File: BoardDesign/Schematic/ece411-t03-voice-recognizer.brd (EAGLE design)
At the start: 92.7 x 63.5 mm, 52 parts, among them J1 5.5x2.1mm Barrel, Q1 16MHz, X1 USB-A

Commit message: asdf
asdasfsadfsfd
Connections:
- net N$7: now also J1.VIN0, SERVO_OUT.1, V_BARREL.TP; no longer TP_USB.TP, X1.1
- net VCC: now also TP_USB.TP, X1.1; no longer J1.VIN0, SERVO_OUT.1, V_BARREL.TP
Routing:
- net VCC: track 295.6 -> 287.8 mm
- net N$7: track 7.74 -> 4.99 mm
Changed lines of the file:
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@@
 <wire x1="53.34" y1="29.87" x2="56.43" y2="29.87" width="0.508" layer="1"/>
 <wire x1="85.09" y1="44.45" x2="82.55" y2="41.91" width="1.27" layer="1"/>
-<contactref element="J1" pad="VIN0"/>
-<contactref element="SERVO_OUT" pad="1"/>
-<contactref element="V_BARREL" pad="TP"/>
 <wire x1="63.5" y1="7.62" x2="63.5" y2="2.54" width="1.27" layer="1"/>
 <wire x1="68.03" y1="23.47" x2="65.43" y2="23.47" width="0.508" layer="1"/>
-<wire x1="95.25" y1="55.23" x2="90.17" y2="55.23" width="1.27" layer="1"/>
-<wire x1="95.25" y1="58.42" x2="96.52" y2="59.69" width="1.27" layer="1"/>
-<wire x1="95.25" y1="58.42" x2="95.25" y2="55.23" width="1.27" layer="1"/>
 <wire x1="90.17" y1="55.23" x2="87.63" y2="52.69" width="1.27" layer="1"/>
-<wire x1="87.63" y1="52.69" x2="87.63" y2="50.8" width="1.27" layer="1"/>
 <contactref element="C9" pad="1"/>
 <contactref element="U$1" pad="44"/>
@@
 <wire x1="35.69" y1="36.83" x2="35.69" y2="52.2" width="1.27" layer="1"/>
 <wire x1="35.69" y1="52.2" x2="38.1" y2="54.61" width="1.27" layer="1"/>
-<wire x1="90.17" y1="48.26" x2="87.63" y2="50.8" width="0.508" layer="1"/>
 <wire x1="54.74" y1="11.43" x2="54.61" y2="11.56" width="0.508" layer="1"/>
 <wire x1="54.74" y1="11.43" x2="57.15" y2="11.43" width="0.508" layer="1"/>
@@
 <via x="90.17" y="39.37" extent="1-16" drill="0.35"/>
 <wire x1="90.17" y1="39.37" x2="90.17" y2="48.26" width="0.508" layer="1"/>
+<contactref element="X1" pad="1"/>
+<contactref element="TP_USB" pad="TP"/>
+<wire x1="90.17" y1="22.86" x2="87.57" y2="20.26" width="0.508" layer="1"/>
+<wire x1="87.57" y1="16.2" x2="87.57" y2="20.26" width="0.508" layer="1"/>
+<wire x1="87.63" y1="52.69" x2="90.17" y2="48.26" width="0" layer="19" extent="1-1"/>
+<wire x1="90.17" y1="22.86" x2="90.17" y2="39.37" width="0" layer="19" extent="1-1"/>
 </signal>
 <signal name="SIGNAL">
@@
 <wire x1="67.31" y1="33.55" x2="67.31" y2="35.56" width="0.508" layer="1"/>
 <wire x1="67.31" y1="35.56" x2="69.85" y2="38.1" width="0.508" layer="1"/>
-</signal>
-<signal name="N$7">
-<contactref element="X1" pad="1"/>
-<contactref element="TP_USB" pad="TP"/>
-<wire x1="90.17" y1="22.86" x2="87.57" y2="20.26" width="0.508" layer="1"/>
-<wire x1="87.57" y1="16.2" x2="87.57" y2="20.26" width="0.508" layer="1"/>
 </signal>
 <signal name="MISO">
@@
 <wire x1="38.1" y1="29.21" x2="35.69" y2="31.75" width="0.508" layer="1"/>
 </signal>
+<signal name="N$7">
+<contactref element="J1" pad="VIN0"/>
+<contactref element="SERVO_OUT" pad="1"/>
+<contactref element="V_BARREL" pad="TP"/>
+<wire x1="95.25" y1="58.42" x2="96.52" y2="59.69" width="1.27" layer="1"/>
+<wire x1="95.25" y1="58.42" x2="95.25" y2="55.23" width="1.27" layer="1"/>
+<wire x1="87.63" y1="50.8" x2="95.25" y2="55.23" width="0" layer="19" extent="1-1"/>
+</signal>
 </signals>

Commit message: Final final finalize finale of the final board layout
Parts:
- removed X1: USB-A, adafruit:MOLEX_480371000
- added J2: USB_MINI-B_SMT, SparkFun-Connectors:USB-MINIB
- moved TP_USB 17.8 mm to (91.4, 5.08)
- moved USB_TO_GND 14.5 mm to (90.2, 17.8)
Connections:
- net GND: now also J2.GND; no longer X1.4
- net N$3: now also J2.D+; no longer X1.3
- net N$9: now also J2.D-; no longer X1.2
- net VCC: now also J2.VBUS; no longer X1.1
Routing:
- net VCC: track 287.8 -> 339.4 mm, vias 4 -> 6
- net GND: track 401.9 -> 388.3 mm
- net N$7: track 4.99 -> 15.5 mm
- net N$9: track 8.37 -> 18.9 mm
- net N$3: track 21.0 -> 23.3 mm, vias 2 -> 1

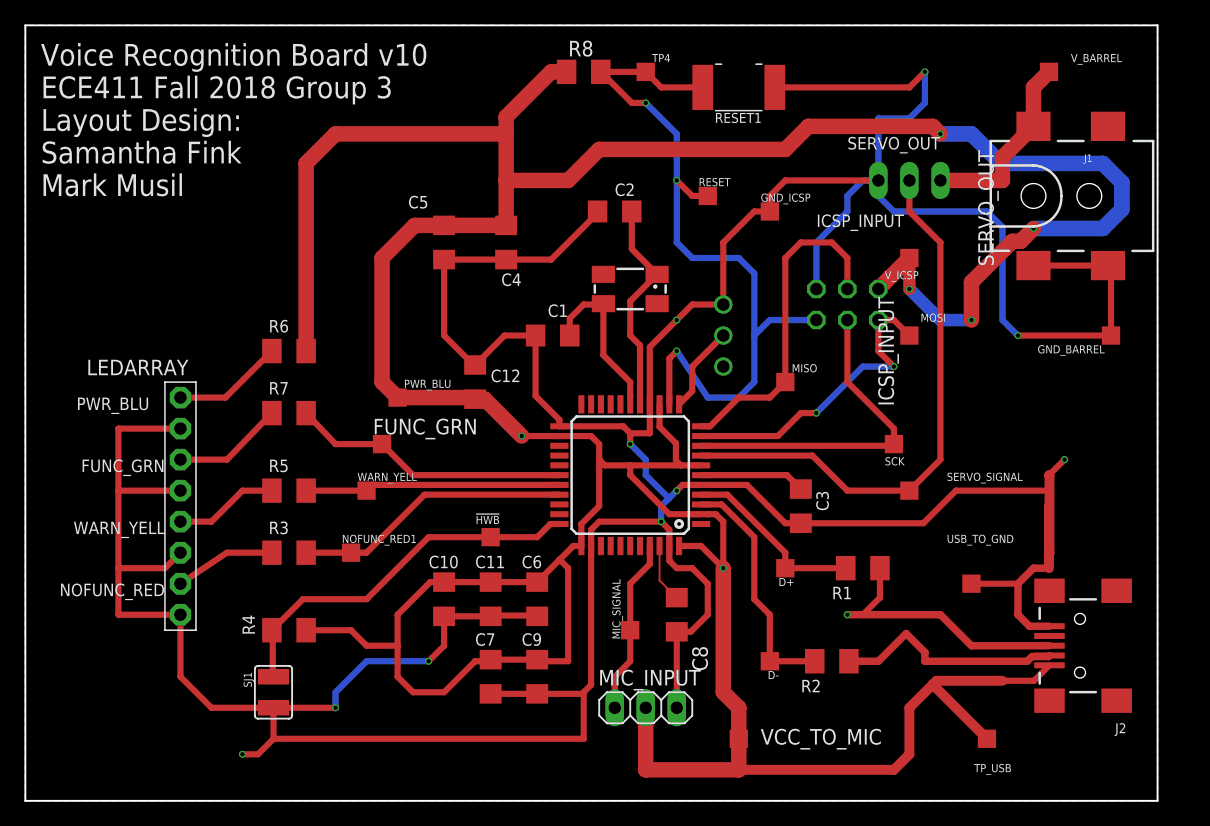
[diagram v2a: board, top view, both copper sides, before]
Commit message: ERC/DRC Checks Complete on new board
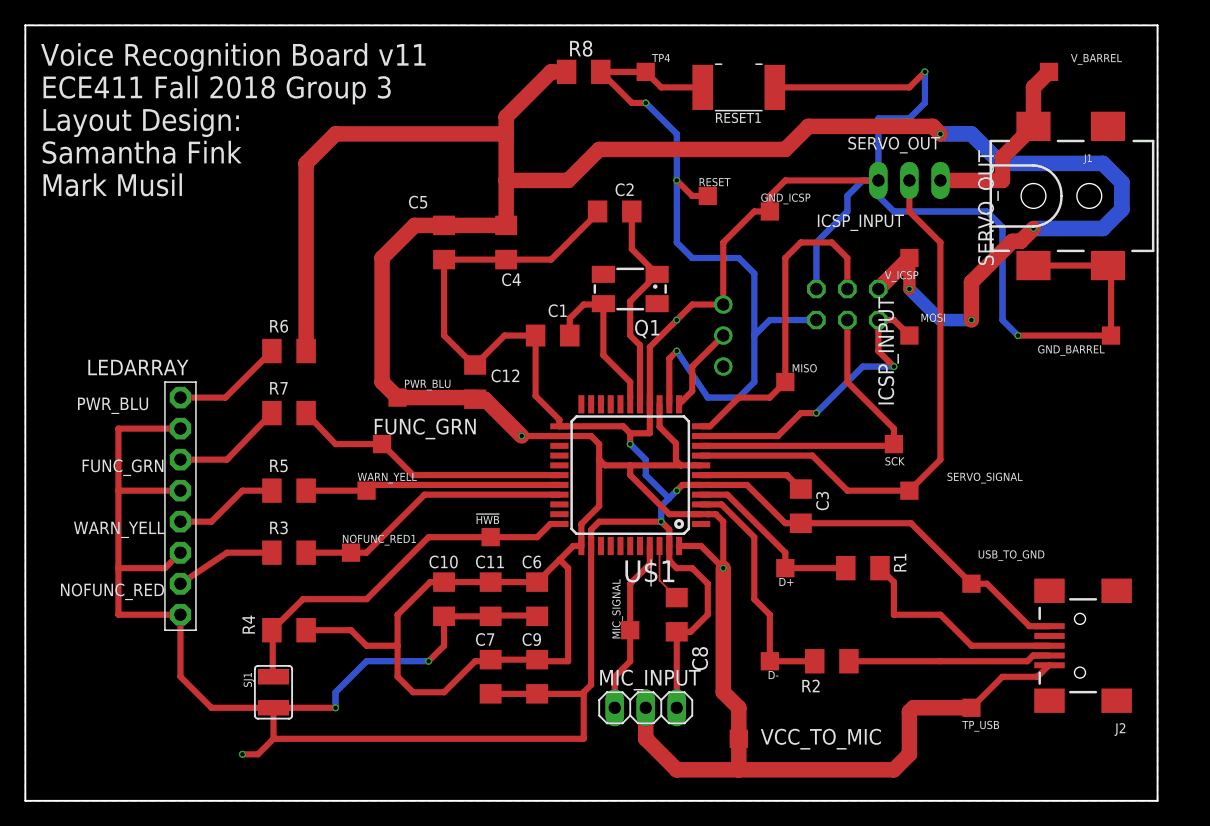
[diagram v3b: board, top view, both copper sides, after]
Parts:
- moved TP_USB 2.84 mm to (90.2, 7.62)
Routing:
- net GND: track 388.3 -> 362.4 mm, vias 10 -> 9
- net VCC: track 339.4 -> 331.4 mm
- net N$3: track 23.3 -> 18.1 mm, vias 1 -> 0
- net N$9: track 18.9 -> 16.6 mm
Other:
- board text added: "Voice Recognition Board v11 ECE411 Fall 2018 Group 3 Layout Design: Samantha Fink Mark Musil"
- board text removed: "Voice Recognition Board v10 ECE411 Fall 2018 Group 3 Layout Design: Samantha Fink Mark Musil"
